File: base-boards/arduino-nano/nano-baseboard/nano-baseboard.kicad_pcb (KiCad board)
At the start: 2 copper layers, 3 parts, among them J1 Conn_02x15_Odd_Even, J2 Conn_02x15_Odd_Even

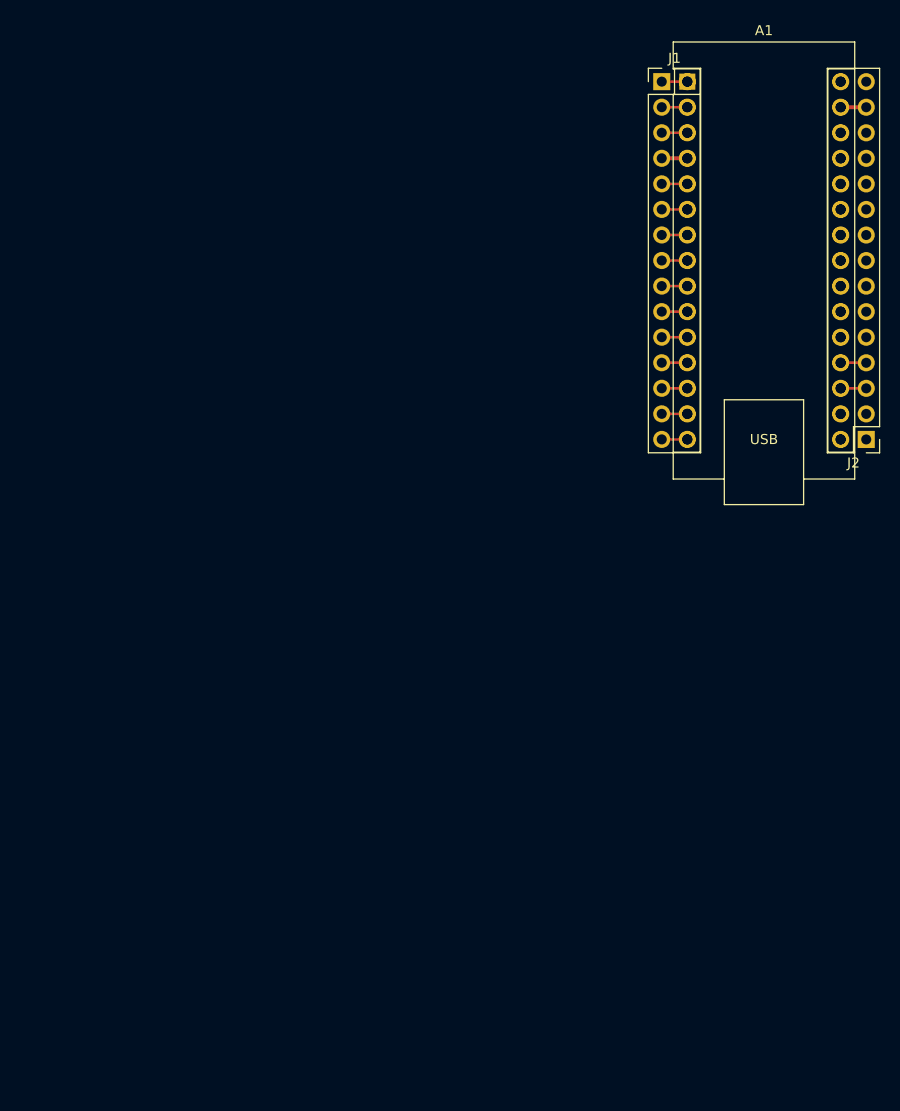
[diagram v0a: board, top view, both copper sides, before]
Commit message: Added Arduino Nano breakout
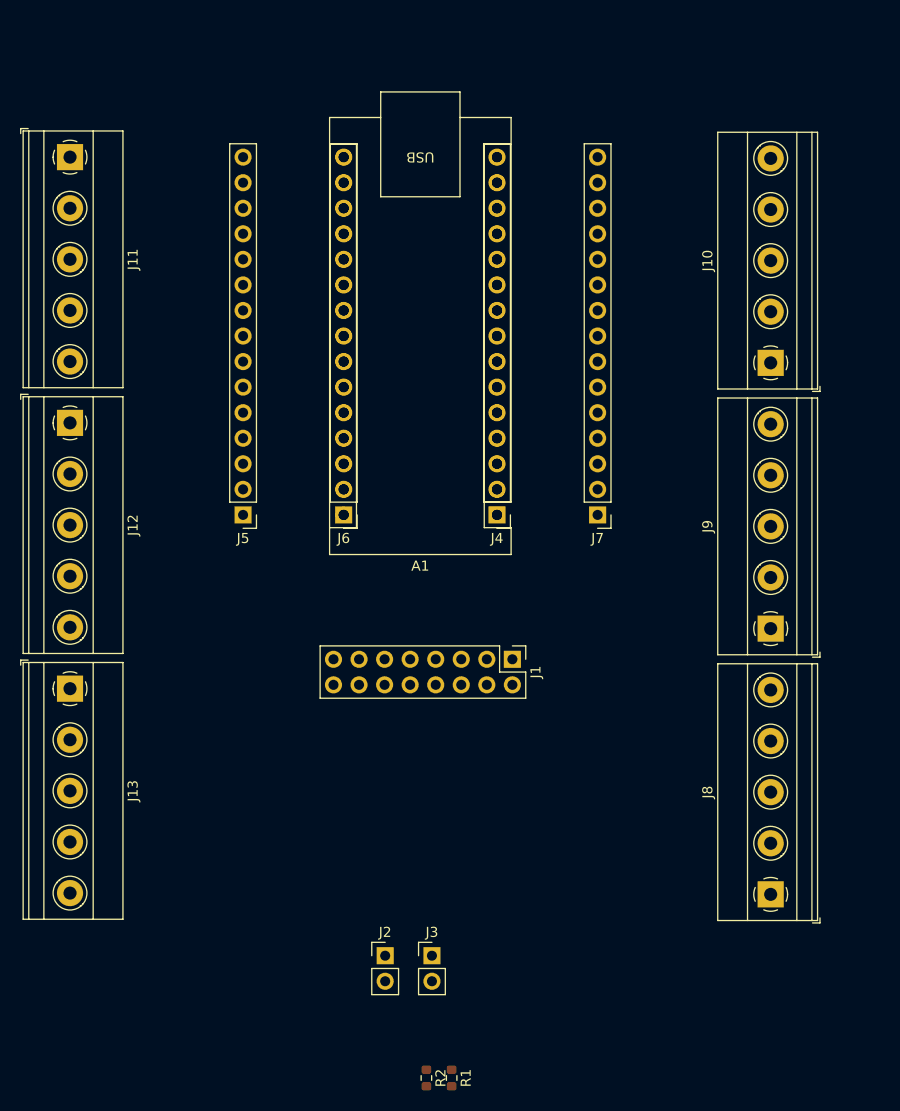
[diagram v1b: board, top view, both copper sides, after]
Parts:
- added J10: Screw_Terminal_01x05, TerminalBlock_Phoenix:TerminalBlock_Phoenix_MKDS-1,5-5-5.08_1x05_P5.08mm_Horizontal, F.Cu at (114.6, 67.3)
- added J11: Screw_Terminal_01x05, TerminalBlock_Phoenix:TerminalBlock_Phoenix_MKDS-1,5-5-5.08_1x05_P5.08mm_Horizontal, F.Cu at (44.9, 46.9)
- added J12: Screw_Terminal_01x05, TerminalBlock_Phoenix:TerminalBlock_Phoenix_MKDS-1,5-5-5.08_1x05_P5.08mm_Horizontal, F.Cu at (44.9, 73.3)
- added J13: Screw_Terminal_01x05, TerminalBlock_Phoenix:TerminalBlock_Phoenix_MKDS-1,5-5-5.08_1x05_P5.08mm_Horizontal, F.Cu at (44.9, 99.7)
- added J3: Conn_01x02_Pin, Connector_PinHeader_2.54mm:PinHeader_1x02_P2.54mm_Vertical, F.Cu at (80.9, 126.2)
- added J4: Conn_01x15, Connector_PinHeader_2.54mm:PinHeader_1x15_P2.54mm_Vertical, F.Cu at (87.4, 82.4)
- added J5: Conn_01x15, Connector_PinHeader_2.54mm:PinHeader_1x15_P2.54mm_Vertical, F.Cu at (62.1, 82.4)
- added J6: Conn_01x15, Connector_PinHeader_2.54mm:PinHeader_1x15_P2.54mm_Vertical, F.Cu at (72.1, 82.4)
- added J7: Conn_01x15, Connector_PinHeader_2.54mm:PinHeader_1x15_P2.54mm_Vertical, F.Cu at (97.4, 82.4)
- added J8: Screw_Terminal_01x05, TerminalBlock_Phoenix:TerminalBlock_Phoenix_MKDS-1,5-5-5.08_1x05_P5.08mm_Horizontal, F.Cu at (114.6, 120.1)
- added J9: Screw_Terminal_01x05, TerminalBlock_Phoenix:TerminalBlock_Phoenix_MKDS-1,5-5-5.08_1x05_P5.08mm_Horizontal, F.Cu at (114.6, 93.7)
- added R1: R_Small_US, Resistor_SMD:R_0603_1608Metric, F.Cu at (82.9, 138.4)
- added R2: R_Small_US, Resistor_SMD:R_0603_1608Metric, F.Cu at (80.3, 138.4)
- J1: value Conn_02x15_Odd_Even -> Conn_02x08_Odd_Even; footprint Connector_PinHeader_2.54mm:PinHeader_2x15_P2.54mm_Vertical -> Connector_PinHeader_2.54mm:PinHeader_2x08_P2.54mm_Vertical
- J2: value Conn_02x15_Odd_Even -> Conn_01x02_Pin; footprint Connector_PinHeader_2.54mm:PinHeader_2x15_P2.54mm_Vertical -> Connector_PinHeader_2.54mm:PinHeader_1x02_P2.54mm_Vertical
- moved J2 70.1 mm to (76.2, 126.2), turned to 0 degrees
- moved J1 59.3 mm to (88.9, 96.8), turned to -90 degrees
- moved A1 47.0 mm to (87.4, 82.4), turned to 180 degrees
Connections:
- A1 pad 1: Net-(A1-Pad1) -> Net-(A1-D1/TX)
- A1 pad 10: Net-(A1-Pad10) -> Net-(A1-D7)
- A1 pad 11: Net-(A1-Pad11) -> Net-(A1-D8)
- A1 pad 12: Net-(A1-Pad12) -> Net-(A1-D9)
- A1 pad 13: Net-(A1-Pad13) -> Net-(A1-D10)
- A1 pad 14: Net-(A1-Pad14) -> SPI_MOSI
- A1 pad 15: Net-(A1-Pad15) -> SPI_MISO
- A1 pad 16: unconnected-(A1-Pad16) -> SPI_SCK
- A1 pad 17: unconnected-(A1-Pad17) -> 3v3
- A1 pad 18: Net-(A1-Pad18) -> Net-(A1-AREF)
- A1 pad 19: Net-(A1-Pad19) -> Net-(A1-A0)
- A1 pad 2: Net-(A1-Pad2) -> Net-(A1-D0/RX)
- A1 pad 20: Net-(A1-Pad20) -> Net-(A1-A1)
- A1 pad 21: Net-(A1-Pad21) -> Net-(A1-A2)
- A1 pad 22: Net-(A1-Pad22) -> Net-(A1-A3)
- A1 pad 23: Net-(A1-Pad23) -> I2C_SDA
- A1 pad 24: Net-(A1-Pad24) -> I2C_SCL
- A1 pad 25: Net-(A1-Pad25) -> Net-(A1-A6)
- A1 pad 26: Net-(A1-Pad26) -> Net-(A1-A7)
- A1 pad 27: unconnected-(A1-Pad27) -> 5v
- A1 pad 5: Net-(A1-Pad5) -> Net-(A1-D2)
- A1 pad 6: Net-(A1-Pad6) -> Net-(A1-D3)
- A1 pad 7: Net-(A1-Pad7) -> Net-(A1-D4)
- A1 pad 8: Net-(A1-Pad8) -> Net-(A1-D5)
- A1 pad 9: Net-(A1-Pad9) -> Net-(A1-D6)
- J1 pad 1: Net-(A1-Pad1) -> 3v3
- J1 pad 10: Net-(A1-Pad5) -> SPI_MISO
- J1 pad 11: Net-(A1-Pad6) -> SPI_SCK
- J1 pad 12: Net-(A1-Pad6) -> unconnected-(J1-Pin_12-Pad12)
- J1 pad 13: Net-(A1-Pad7) -> unconnected-(J1-Pin_13-Pad13)
- J1 pad 14: Net-(A1-Pad7) -> unconnected-(J1-Pin_14-Pad14)
- J1 pad 15: Net-(A1-Pad8) -> unconnected-(J1-Pin_15-Pad15)
- J1 pad 16: Net-(A1-Pad8) -> unconnected-(J1-Pin_16-Pad16)
- J1 pad 2: Net-(A1-Pad1) -> 3v3
- J1 pad 3: Net-(A1-Pad2) -> 5v
- J1 pad 4: Net-(A1-Pad2) -> 5v
- J1 pad 5: RST -> GND
- J1 pad 6: RST -> GND
- J1 pad 7: GND -> I2C_SDA
- J1 pad 8: GND -> I2C_SCL
- J1 pad 9: Net-(A1-Pad5) -> SPI_MOSI
- J2 pad 1: Net-(J2-Pad1) -> 5v
- J2 pad 2: Net-(J2-Pad1) -> Net-(J2-Pin_2)
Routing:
- net GND: track 5.09 -> 0.01 mm
- net Net-(A1-Pad19): track 2.55 -> 0.00 mm
- net RST: track 2.54 -> 0.00 mm
- net Net-(A1-Pad9): track 2.54 -> 0.00 mm
- net Net-(A1-Pad8): track 2.54 -> 0.00 mm
- net Net-(A1-Pad7): track 2.54 -> 0.00 mm
- net Net-(A1-Pad6): track 2.54 -> 0.00 mm
- net Net-(A1-Pad5): track 2.54 -> 0.00 mm
- net Net-(A1-Pad2): track 2.54 -> 0.00 mm
- net Net-(A1-Pad15): track 2.54 -> 0.00 mm
- net Net-(A1-Pad14): track 2.54 -> 0.00 mm
- net Net-(A1-Pad13): track 2.54 -> 0.00 mm
- net Net-(A1-Pad12): track 2.54 -> 0.00 mm
- net Net-(A1-Pad11): track 2.54 -> 0.00 mm
- net Net-(A1-Pad10): track 2.54 -> 0.00 mm
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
